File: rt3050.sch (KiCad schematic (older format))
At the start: 0 parts

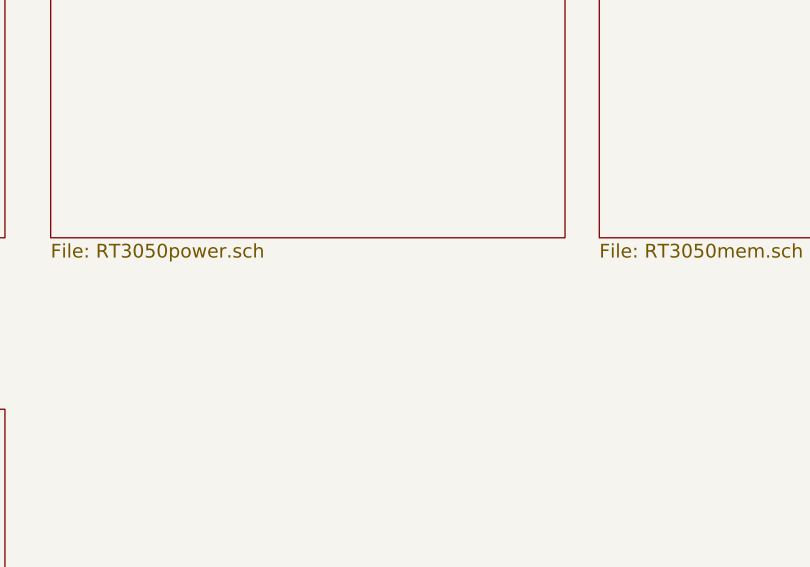
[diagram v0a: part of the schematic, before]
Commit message: updated component values
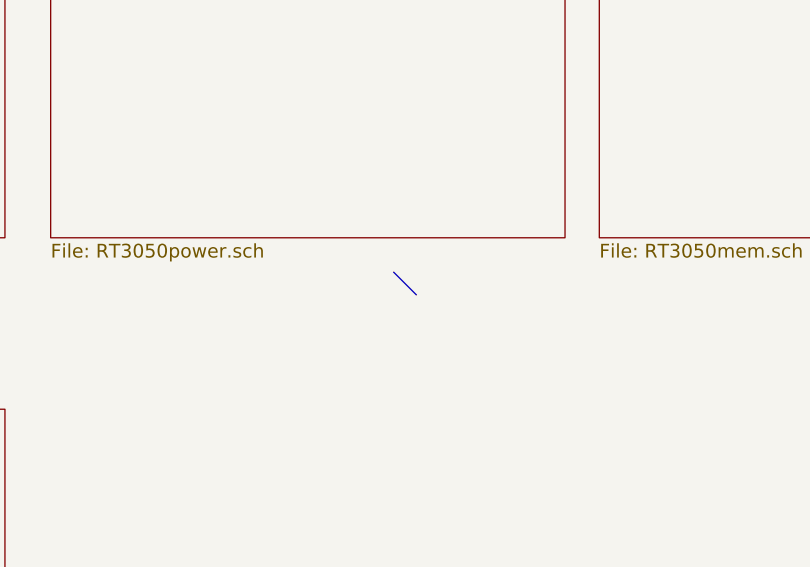
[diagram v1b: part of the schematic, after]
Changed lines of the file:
@@
-EESchema Schematic File Version 2  date Tue 02 Sep 2014 15:48:53 BST
+EESchema Schematic File Version 2
 LIBS:power
 LIBS:device
@@
 LIBS:AIC809
 LIBS:rt3050-cache
-EELAYER 25  0
+EELAYER 25 0
 EELAYER END
-$Descr A4 11700 8267
+$Descr A4 11693 8268
 encoding utf-8
 Sheet 1 6
@@
 F1 "RT3050main.sch" 60
 $EndSheet
+Entry Bus Bus
+	4650 2900 4750 3000
 $EndSCHEMATC
